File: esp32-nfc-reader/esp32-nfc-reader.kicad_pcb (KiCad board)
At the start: 4 copper layers, 46 x 89.5 mm, 55 parts, among them J1 USB_C_Receptacle_USB2.0_16P, J2 Conn_01x02_Pin, J3 Conn_01x08, K1 Relay_SPDT, Q1 PMOS, Q2 Q_NMOS, SW1 RESET, SW2 BOOT, SW3 USER_INPUT, U1 ESP32-S3-WROOM-1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

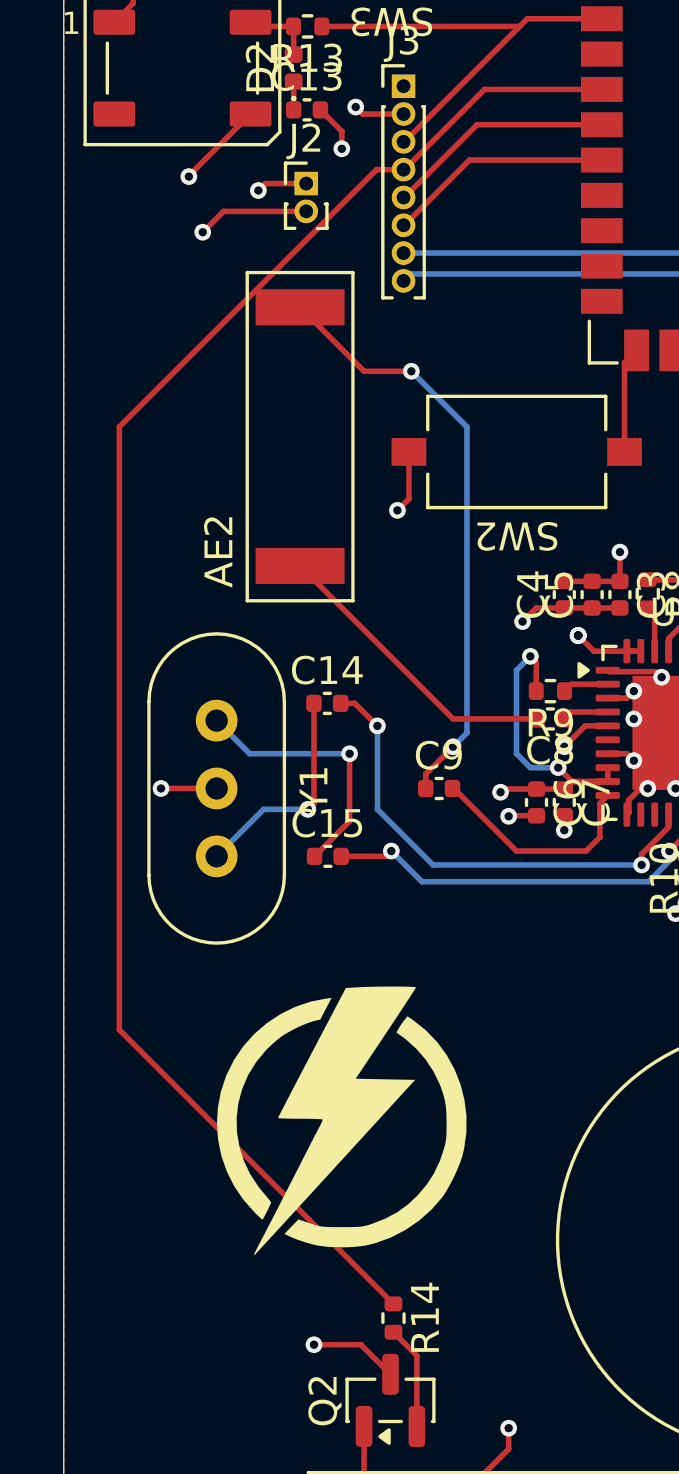
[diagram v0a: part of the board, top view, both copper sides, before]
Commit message: fixed some issues with pcb
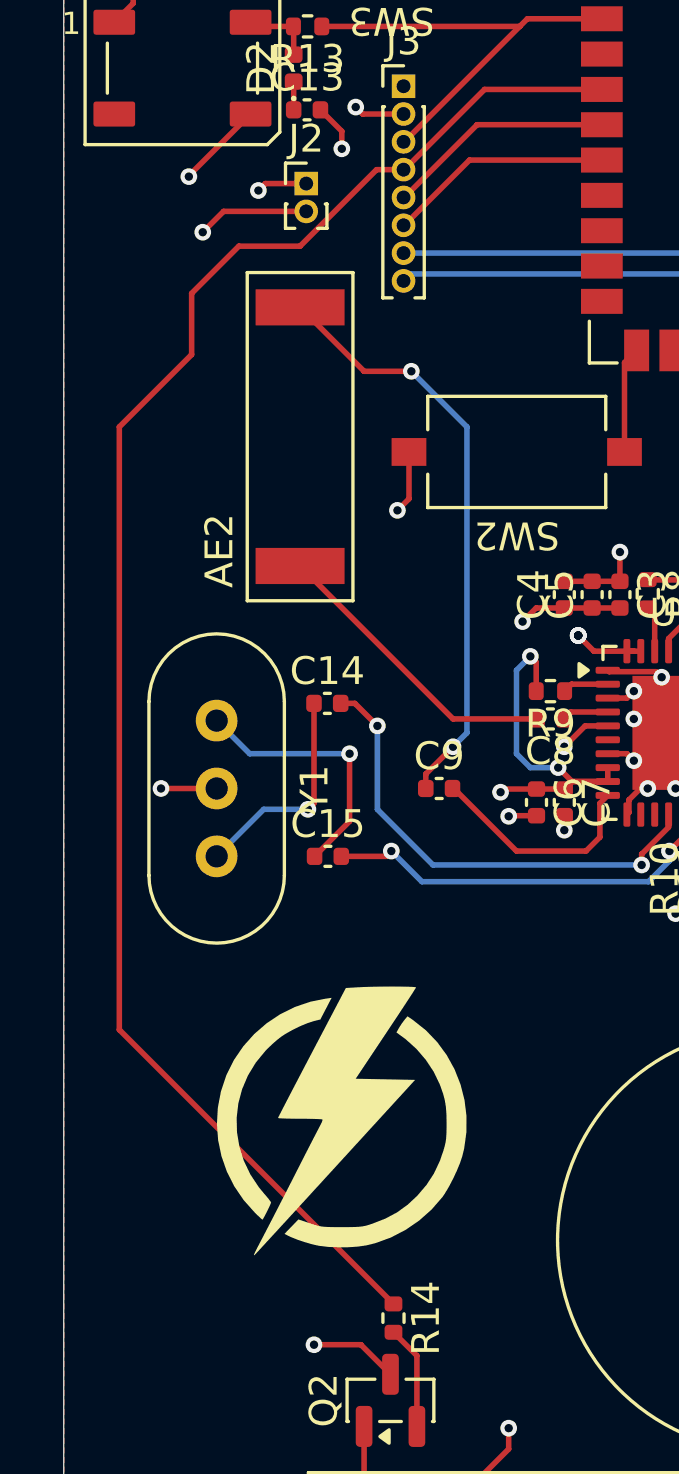
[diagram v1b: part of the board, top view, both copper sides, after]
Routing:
- net /IO12: track 58.0 -> 59.3 mm
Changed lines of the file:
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@@
-		)
-	)
-	(dimension
-		(type orthogonal)
-		(layer "Edge.Cuts")
-		(pts
-			(xy 122.5 135) (xy 122.5 45.5)
-		)
-		(height -15.5)
-		(orientation 1)
-		(format
-			(prefix "")
-			(suffix "")
-			(units 3)
-			(units_format 0)
-			(precision 4)
-			(suppress_zeroes yes)
-		)
-		(style
-			(thickness 0.05)
-			(arrow_length 1.27)
-			(text_position_mode 0)
-			(arrow_direction outward)
-			(extension_height 0.58642)
-			(extension_offset 0.5)
-			(keep_text_aligned yes)
-		)
-		(gr_text "89.5"
-			(at 105.85 90.25 90)
-			(layer "Edge.Cuts")
-			(effects
-				(font
-					(size 1 1)
-					(thickness 0.15)
-				)
-			)
-		)
-	)
-	(dimension
-		(type orthogonal)
-		(layer "Edge.Cuts")
-		(pts
-			(xy 122.5 135) (xy 168.5 135)
-		)
-		(height 6)
-		(orientation 0)
-		(format
-			(prefix "")
-			(suffix "")
-			(units 3)
-			(units_format 0)
-			(precision 4)
-			(suppress_zeroes yes)
-		)
-		(style
-			(thickness 0.05)
-			(arrow_length 1.27)
-			(text_position_mode 0)
-			(arrow_direction outward)
-			(extension_height 0.58642)
-			(extension_offset 0.5)
-			(keep_text_aligned yes)
-		)
-		(gr_text "46"
-			(at 145.5 139.85 0)
-			(layer "Edge.Cuts")
-			(effects
-				(font
-					(size 1 1)
-					(thickness 0.15)
-				)
-			)
 		)
 	)
@@
 	)
 	(segment
-		(start 133.75 81.25)
-		(end 134.72 81.25)
+		(start 134.72 81.25)
+		(end 133.75 81.25)
+		(width 0.2)
+		(layer "F.Cu")
+		(net 32)
+	)
+	(segment
+		(start 124.5 112.175)
+		(end 134.3575 122.0325)
+		(width 0.2)
+		(layer "F.Cu")
+		(net 32)
+	)
+	(segment
+		(start 124.5 90.5)
+		(end 124.5 112.175)
+		(width 0.2)
+		(layer "F.Cu")
+		(net 32)
+	)
+	(segment
+		(start 127.1 87.9)
+		(end 124.5 90.5)
 		(width 0.2)
 		(layer "F.Cu")
@@
 	)
 	(segment
-		(start 134.3575 122.0325)
-		(end 124.5 112.175)
+		(start 133.75 81.25)
+		(end 131 84)
 		(width 0.2)
 		(layer "F.Cu")
@@
 	)
 	(segment
-		(start 124.5 90.5)
-		(end 133.75 81.25)
+		(start 131 84)
+		(end 128.8 84)
+		(width 0.2)
+		(layer "F.Cu")
+		(net 32)
+	)
+	(segment
+		(start 127.1 85.7)
+		(end 127.1 87.9)
+		(width 0.2)
+		(layer "F.Cu")
+		(net 32)
+	)
+	(segment
+		(start 128.8 84)
+		(end 127.1 85.7)
 		(width 0.2)
 		(layer "F.Cu")
@@
 		(width 0.2)
 		(layer "F.Cu")
-		(net 32)
-	)
-	(segment
-		(start 124.5 112.175)
-		(end 124.5 90.5)
-		(width 0.2)
-		(layer "F.Cu")
